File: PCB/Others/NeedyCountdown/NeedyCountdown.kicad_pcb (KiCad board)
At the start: 2 copper layers, 23 x 35 mm, 18 parts, among them J1 3V3, J2 LAT, J3 SCLK, J4 SIN, J5 BLANK, J6 SCL, J7 SDA, J8 GND, U3 AD5272BRMZ-50, U4 TLC59281

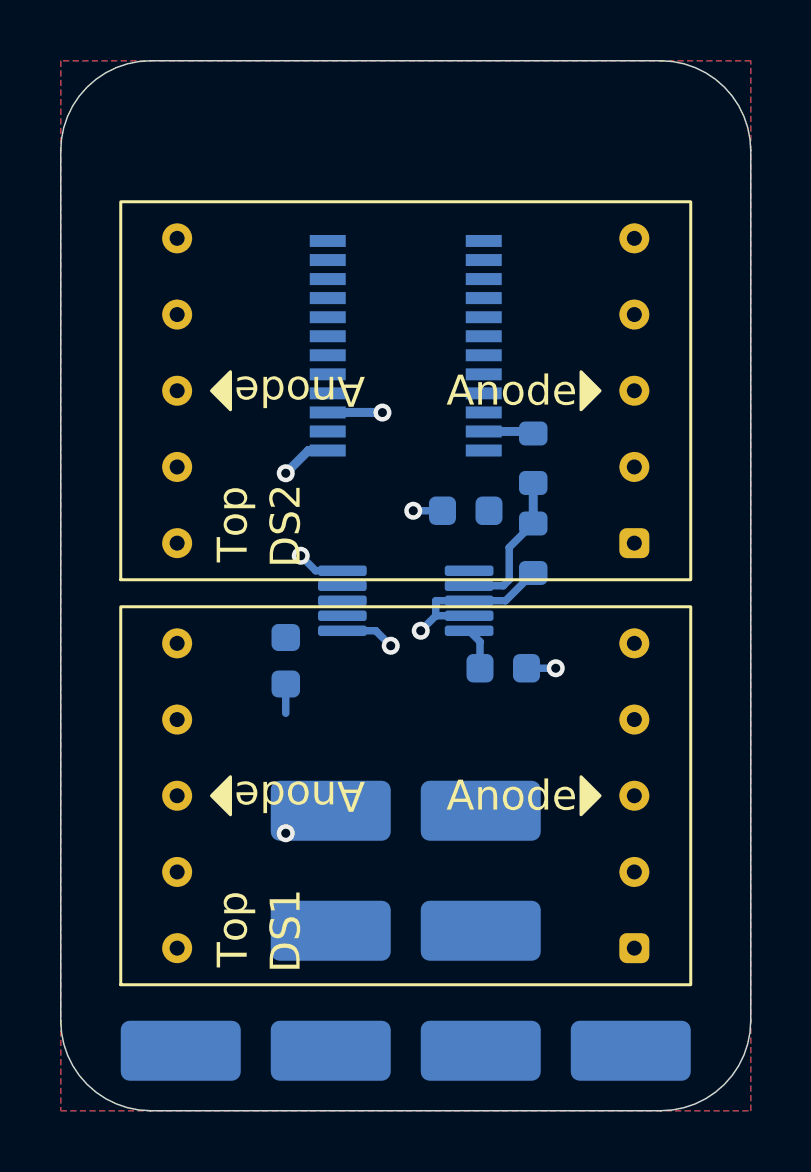
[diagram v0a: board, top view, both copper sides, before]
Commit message: feat: Add single WS2812 ARGB break out board
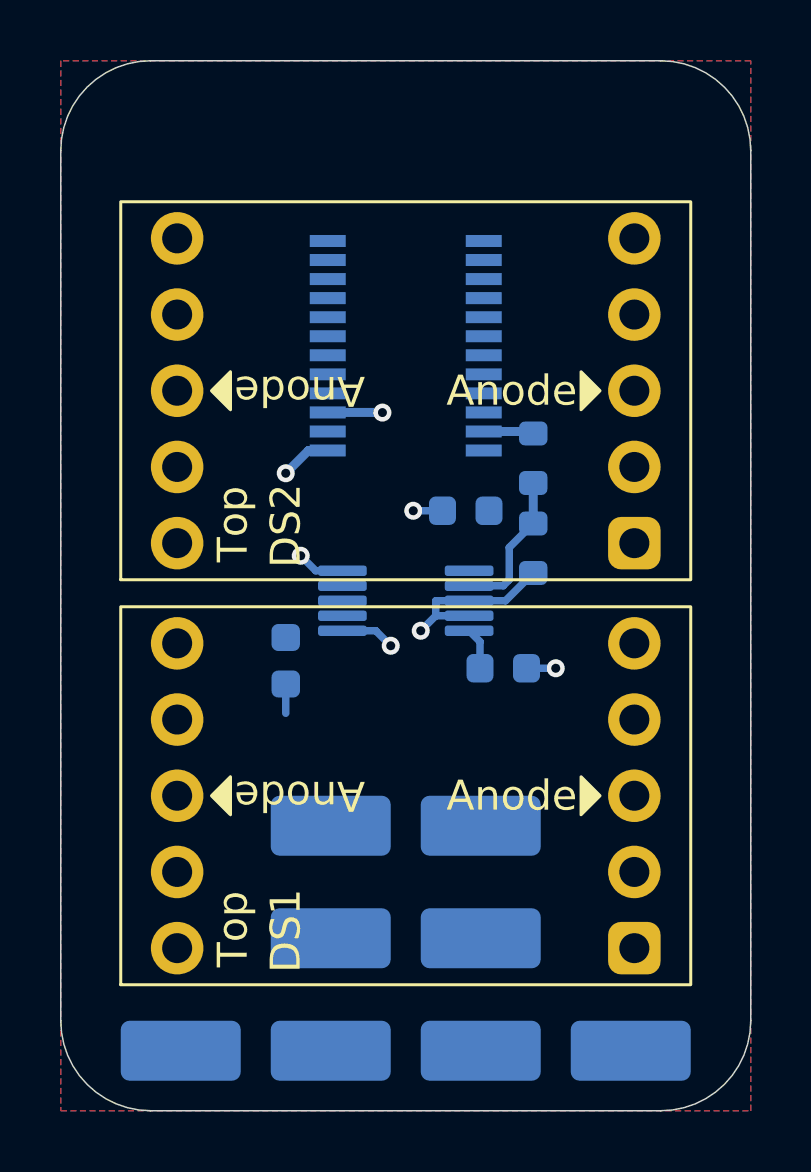
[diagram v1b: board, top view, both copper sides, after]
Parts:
- removed the G*** at (39.3, 22.9)
- added G***: LOGO, KTANE:KTANEIRL-0303, B.Cu at (39.2, 22.2)
- moved J1 12.8 mm to (24.0, 53.0)
- moved J8 12.8 mm to (39.0, 53.0)
- moved J6 10.7 mm to (34.0, 49.2)
- moved J2 10.0 mm to (29.0, 53.0)
- moved J7 9.01 mm to (34.0, 45.5)
- moved J3 5.01 mm to (29.0, 49.2)
- moved J4 3.50 mm to (29.0, 45.5)
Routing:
- net GND: vias 7 -> 6

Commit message: feat: Audio playback in chassis, including custom FAT for sdcard.
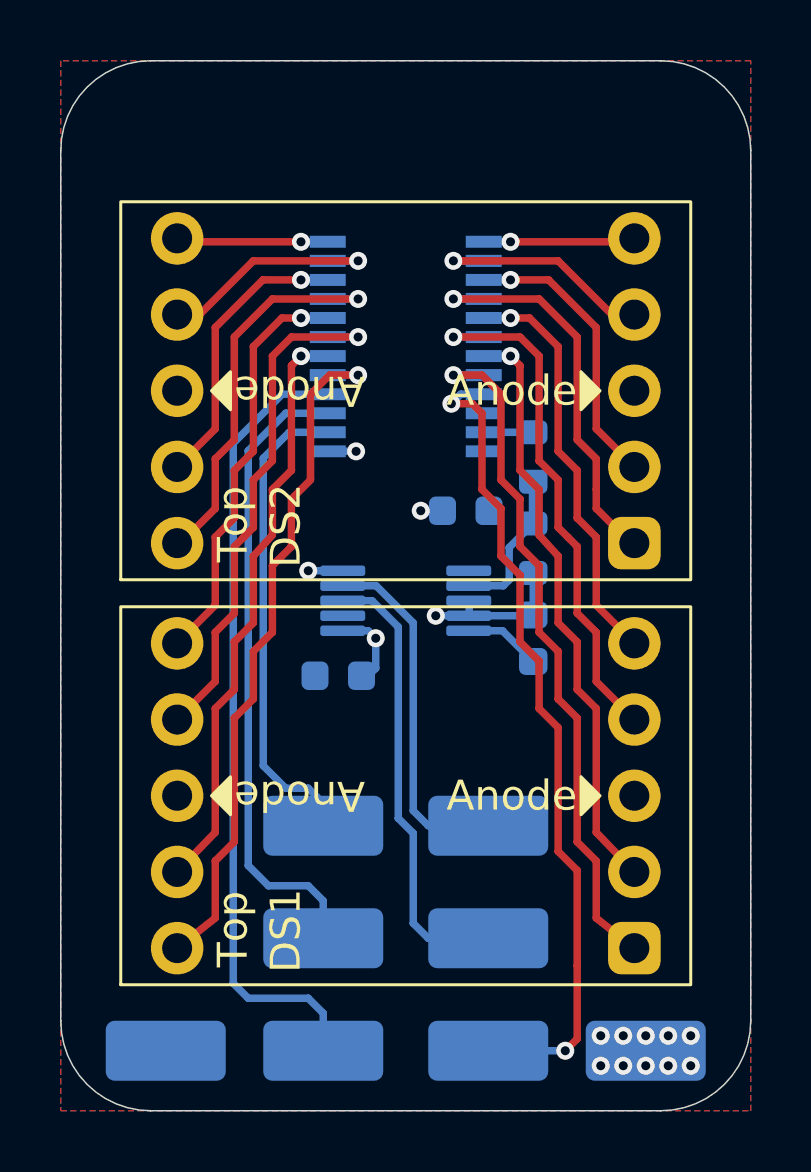
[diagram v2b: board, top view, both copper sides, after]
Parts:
- moved C4 1.82 mm to (29.2, 40.5), turned to 0 degrees
- moved C6 1.41 mm to (35.8, 39.2), turned to 90 degrees
- moved J1 0.50 mm to (23.5, 53.0)
- moved J8 0.50 mm to (39.5, 53.0)
- moved J2 0.25 mm to (28.8, 53.0)
- moved J3 0.25 mm to (28.8, 49.2)
- moved J4 0.25 mm to (28.8, 45.5)
- moved J5 0.25 mm to (34.2, 53.0)
- moved J6 0.25 mm to (34.2, 49.2)
- moved J7 0.25 mm to (34.2, 45.5)
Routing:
- net BLANK: track 0.00 -> 27.7 mm, vias 0 -> 2
- net LAT: track 0.00 -> 26.6 mm
- net /DS1G: track 0.00 -> 23.3 mm, vias 0 -> 1
- net /DS1E: track 0.00 -> 23.3 mm, vias 0 -> 1
- net /DS1F: track 0.00 -> 19.8 mm, vias 0 -> 1
- net /DS1D: track 0.00 -> 19.8 mm, vias 0 -> 1
- net SCLK: track 1.82 -> 21.2 mm, vias 1 -> 0
- net /DS1A: track 0.00 -> 17.6 mm, vias 0 -> 1
- net /DS1C: track 0.00 -> 17.6 mm, vias 0 -> 1
- net SIN: track 0.00 -> 16.0 mm
- net I2CDAT: track 0.00 -> 15.0 mm
- net /DS1B: track 0.00 -> 13.8 mm, vias 0 -> 1
- net /DS1DP: track 0.00 -> 13.8 mm, vias 0 -> 1
- net /DS2G: track 0.00 -> 13.4 mm, vias 0 -> 1
- net /DS2E: track 0.00 -> 13.3 mm, vias 0 -> 1
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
